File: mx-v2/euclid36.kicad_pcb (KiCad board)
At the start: 2 copper layers, 248.2 x 127 mm, 114 parts, among them SW1 RotaryEncoder_Switch, SW10 SW_PUSH, SW11 SW_PUSH, SW12 SW_PUSH, SW14 SW_PUSH, SW15 SW_PUSH, SW16 SW_PUSH, SW17 SW_PUSH, SW18 SW_PUSH, SW19 SW_PUSH, SW2 SW_PUSH, SW20 SW_PUSH, SW21 SW_PUSH, SW22 SW_PUSH, SW23 SW_PUSH, SW25 SW_PUSH, SW26 SW_PUSH, SW27 SW_PUSH, SW28 SW_PUSH, SW29 SW_PUSH, SW3 SW_PUSH, SW31 SW_PUSH, SW32 SW_PUSH, SW33 SW_PUSH, SW34 SW_PUSH, SW35 SW_PUSH, SW37 SW_PUSH, SW38 SW_PUSH, SW39 SW_PUSH, SW4 SW_PUSH, SW40 SW_PUSH, SW41 SW_PUSH, SW42 SW_PUSH, SW5 SW_PUSH, SW6 SW_PUSH, SW7 RotaryEncoder_Switch, SW8 SW_PUSH, SW9 SW_PUSH, U1 USBLC6-2SC6, U2 ATmega32U4-AU, Y1 XTAL

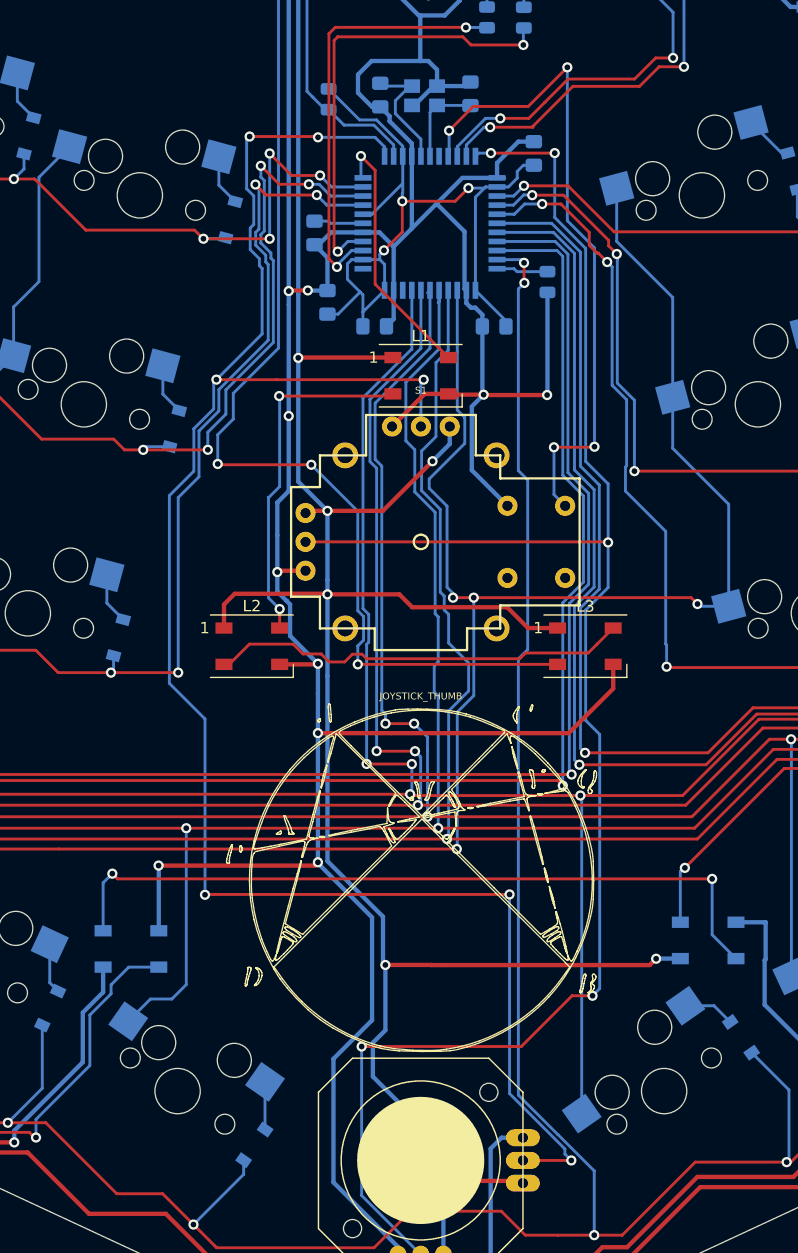
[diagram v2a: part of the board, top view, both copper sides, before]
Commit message: accidentally wired my analog joysticks to digital inputs
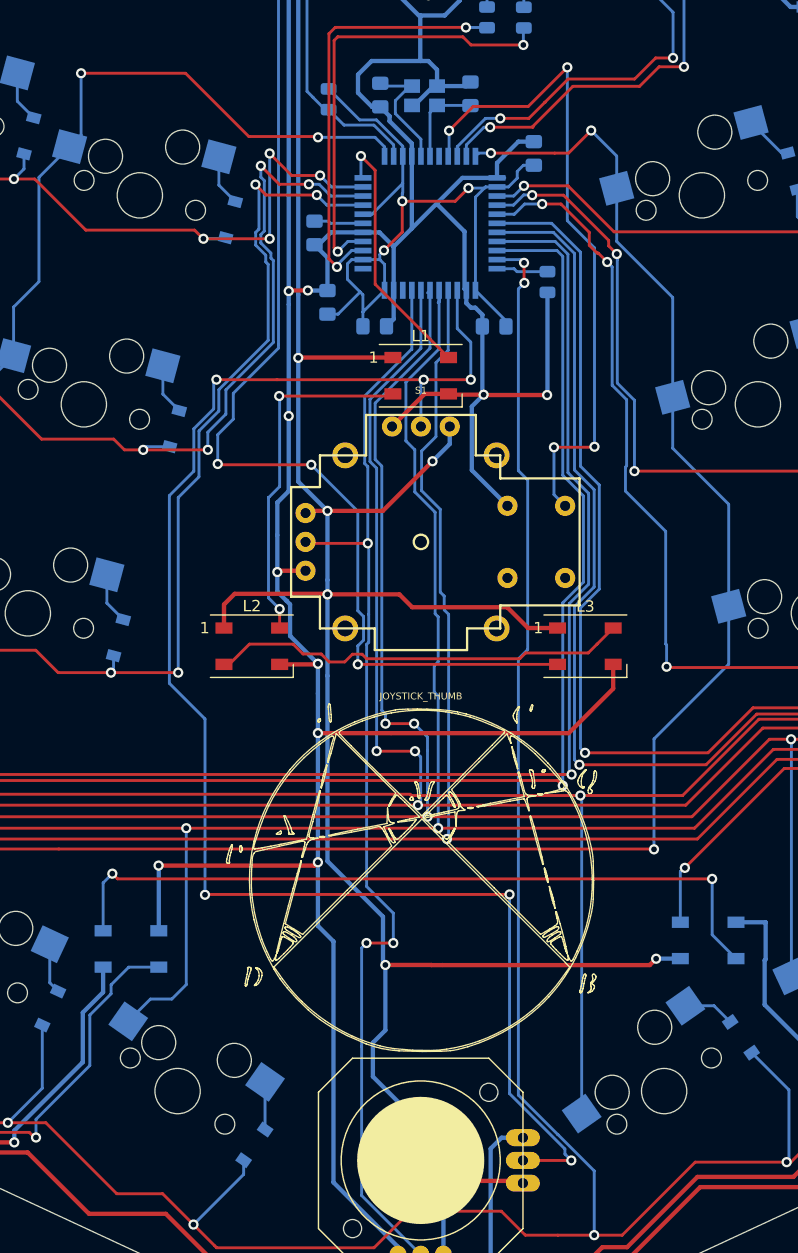
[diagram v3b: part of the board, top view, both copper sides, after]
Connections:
- U2 pad 12: Net-(JOY1-PadX) -> col5
- U2 pad 22: Net-(JOY1-PadY) -> col0
- U2 pad 36: col0 -> Net-(JOY1-PadX)
- U2 pad 41: col5 -> Net-(JOY1-PadY)
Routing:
- net Net-(JOY1-PadY): track 154.9 -> 98.8 mm, vias 5 -> 3
- net Net-(JOY1-PadX): track 164.7 -> 140.1 mm, vias 7 -> 6
- net col0: track 234.4 -> 216.2 mm, vias 6 -> 5
- net col5: track 294.6 -> 281.2 mm, vias 6 -> 5
- net GND: track 1162.7 -> 1160.0 mm
- net col1: track 355.6 -> 354.2 mm

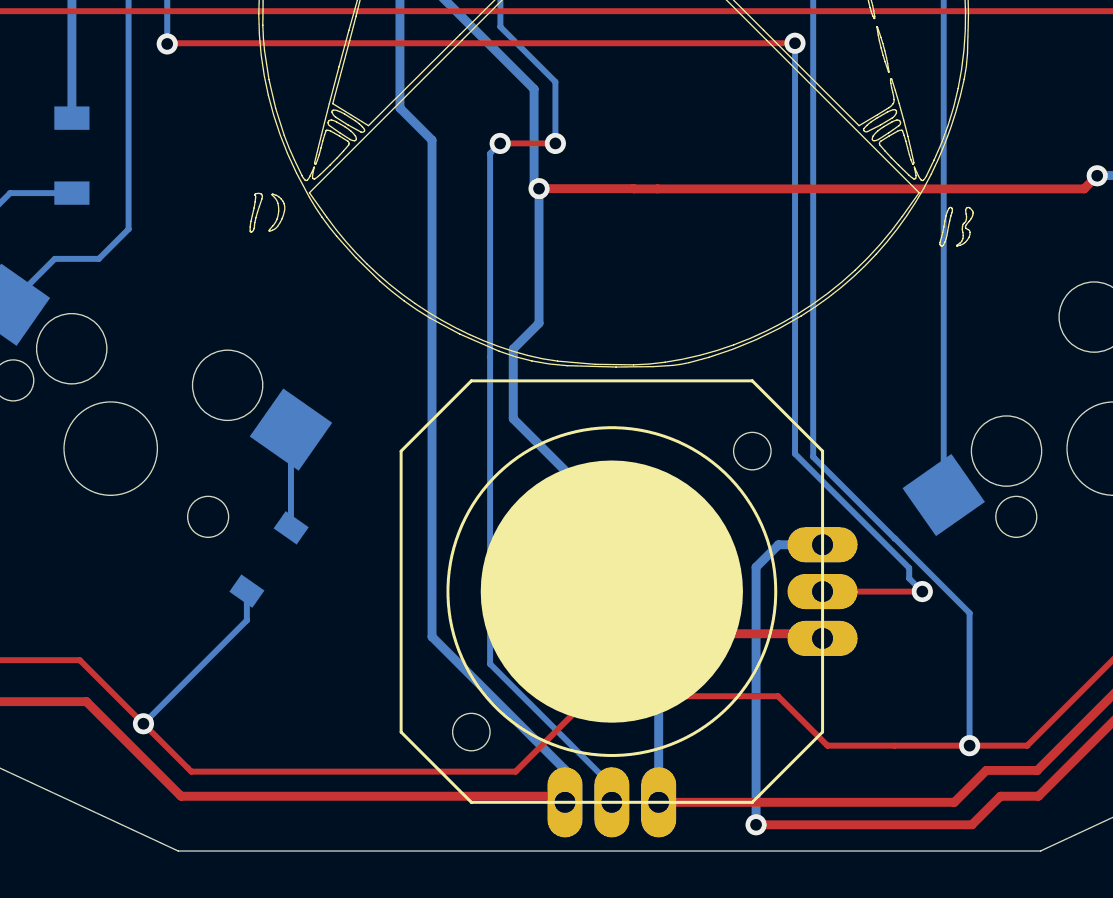
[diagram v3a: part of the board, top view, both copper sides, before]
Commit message: added support for another joystick type, psp, as well as readme update with new feature layout image
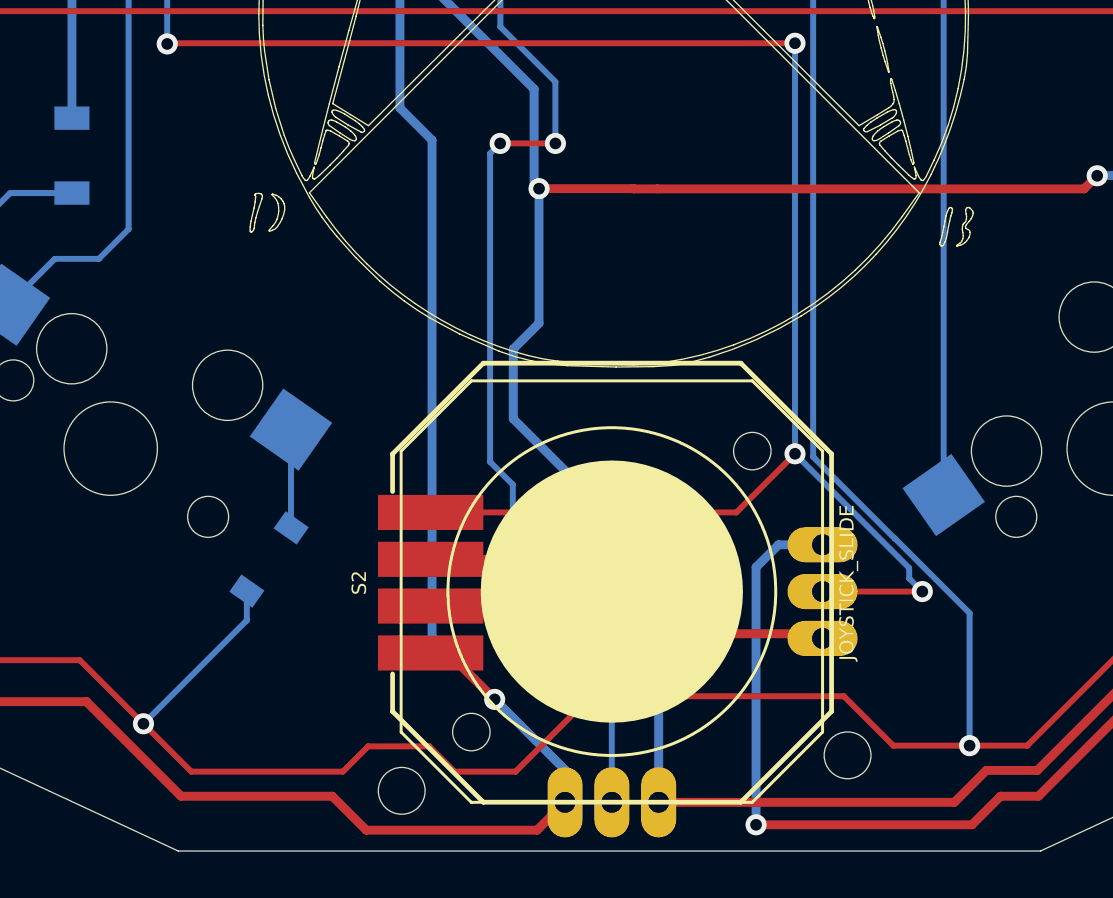
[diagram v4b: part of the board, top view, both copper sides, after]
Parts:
- added S2: JOYSTICK_SLIDE, SparkFun-Switches:JOYSTICK-PSP1000, F.Cu at (150.6, 140.9)
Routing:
- net Net-(JOY1-PadX): track 140.1 -> 156.7 mm, vias 6 -> 7
- net VCC: track 918.6 -> 928.7 mm
- net GND: track 1160.0 -> 1164.9 mm, vias 31 -> 32
- net Net-(JOY1-PadY): track 98.8 -> 103.0 mm, vias 3 -> 4
- net row6: track 296.2 -> 297.1 mm

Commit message: Proto V2 complete and ordered from jlcpcb.com
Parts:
- added REF**: M2_Hole_NPTH_Outside, _reviung-kbd:M2_Hole_NPTH_Outside, F.Cu at (150.8, 127.7)
- added REF**: M2_Hole_NPTH_Outside, _reviung-kbd:M2_Hole_NPTH_Outside, F.Cu at (251.9, 94.5)
- added REF**: M2_Hole_NPTH_Outside, _reviung-kbd:M2_Hole_NPTH_Outside, F.Cu at (51.1, 94.4)
- added REF**: M2_Hole_NPTH_Outside, _reviung-kbd:M2_Hole_NPTH_Outside, F.Cu at (249.7, 31.4)
- added REF**: M2_Hole_NPTH_Outside, _reviung-kbd:M2_Hole_NPTH_Outside, F.Cu at (176.2, 35.6)
- added REF**: M2_Hole_NPTH_Outside, _reviung-kbd:M2_Hole_NPTH_Outside, F.Cu at (124.6, 35.2)
- added REF**: M2_Hole_NPTH_Outside, _reviung-kbd:M2_Hole_NPTH_Outside, F.Cu at (51.9, 31.4)

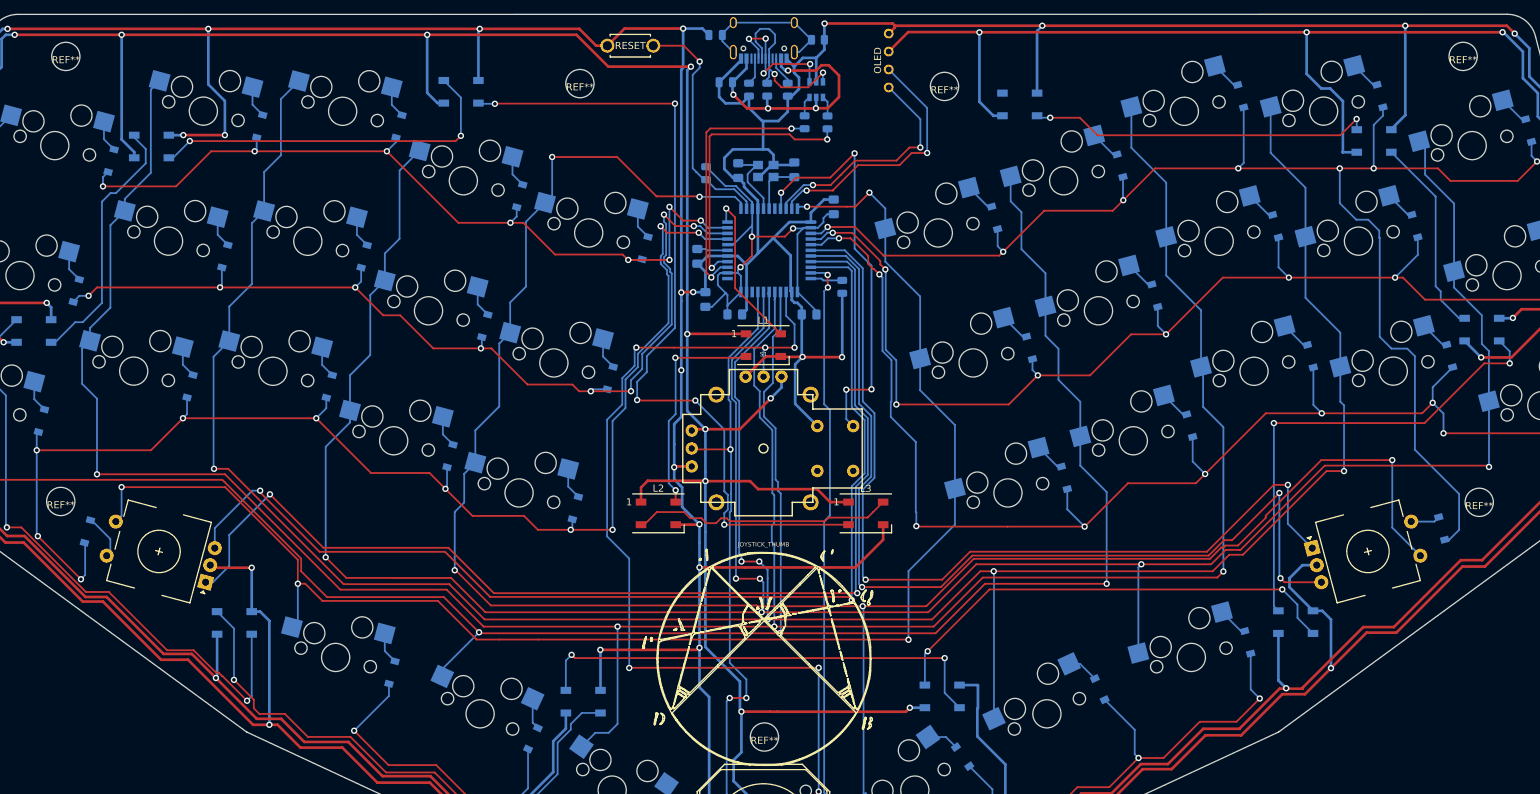
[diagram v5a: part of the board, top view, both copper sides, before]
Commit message: last revision had a few problems, fixed some, see todo.txt
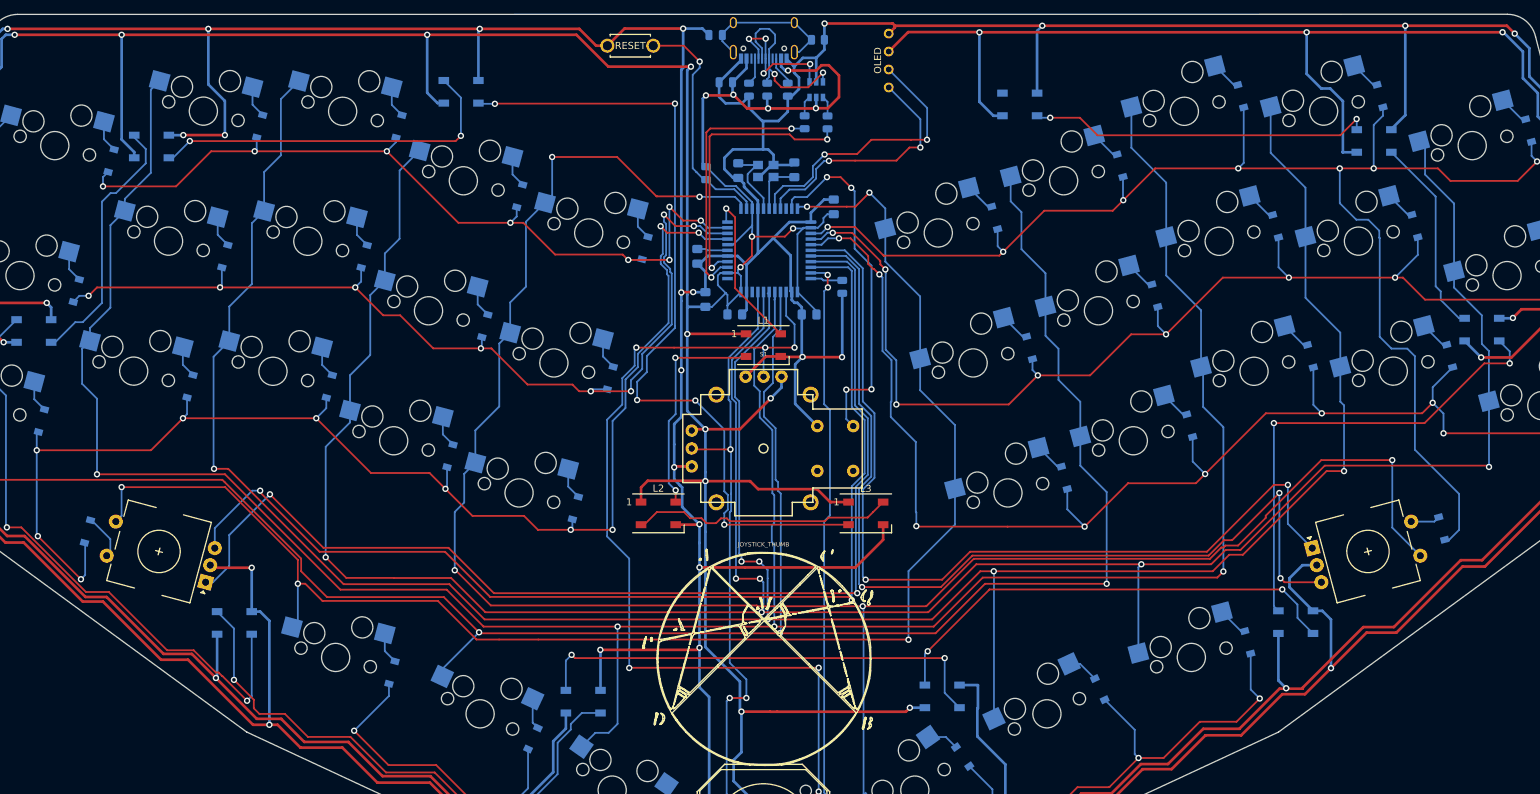
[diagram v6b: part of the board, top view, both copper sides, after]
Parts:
- removed REF** (x7): M2_Hole_NPTH_Outside, _reviung-kbd:M2_Hole_NPTH_Outside
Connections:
- C2 pad 1: +5V -> VBUS
- C3 pad 1: +5V -> VBUS
- C4 pad 1: +5V -> VBUS
- C5 pad 1: +5V -> VBUS
- JOY1 pad X+: VCC -> VBUS
- JOY1 pad Y+: VCC -> VBUS
- L1 pad 1: VCC -> VBUS
- L10 pad 1: VCC -> VBUS
- L11 pad 1: VCC -> VBUS
- L12 pad 1: VCC -> VBUS
- L13 pad 1: VCC -> VBUS
- L2 pad 1: VCC -> VBUS
- L3 pad 1: VCC -> VBUS
- L4 pad 1: VCC -> VBUS
- L5 pad 1: VCC -> VBUS
- L6 pad 1: VCC -> VBUS
- L7 pad 1: VCC -> VBUS
- L8 pad 1: VCC -> VBUS
- L9 pad 1: VCC -> VBUS
- OL1 pad 3: VCC -> VBUS
- R2 pad 1: +5V -> VBUS
- S1 pad H1: VCC -> VBUS
- S1 pad V1: VCC -> VBUS
- S2 pad VCC: VCC -> VBUS
- U2 pad 14: +5V -> VBUS
- U2 pad 18: Net-(U2-Pad18) -> SCL
- U2 pad 19: Net-(S1-PadB1A) -> SDA
- U2 pad 2: +5V -> VBUS
- U2 pad 20: SDA -> Net-(U2-Pad20)
- U2 pad 21: SCL -> Net-(S1-PadB1A)
- U2 pad 24: +5V -> VBUS
- U2 pad 34: +5V -> VBUS
- U2 pad 44: +5V -> VBUS
- U2 pad 7: +5V -> VBUS
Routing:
- net VBUS: track 39.3 -> 1054.4 mm, vias 4 -> 31
- net VCC: track 928.7 -> 0.00 mm, vias 23 -> 0
- net +5V: track 69.4 -> 0.00 mm, vias 3 -> 0
- net Net-(S1-PadB1A): track 58.6 -> 50.5 mm
- net SCL: track 37.1 -> 39.9 mm
- net SDA: track 33.5 -> 35.5 mm
